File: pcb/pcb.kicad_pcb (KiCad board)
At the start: 2 copper layers, 99.7 x 99.7 mm, 47 parts, among them IC1 TPS63802DLAT, IC2 TUSB320LIRWBR, J1 USB_C_Receptacle_PowerOnly_6P, J2 Soil_Sensor, J3 Pump, J4 Conn_01x03, Q1 2N7002, Q2 AO3401A, Q3 AO3400A, U1 BQ24075RGTR, U2 ESP-32S_USB-C_CH340_DevBoard

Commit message: Testing some KiCAD preview (PCB, Schematic) and checks (ERC, DRC) automation
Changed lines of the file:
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@@
 		(tags "resistor handsolder")
 		(property "Reference" "R14"
-			(at -4.318 0 0)
+			(at 0 2.032 0)
 			(layer "F.SilkS")
 			(effects

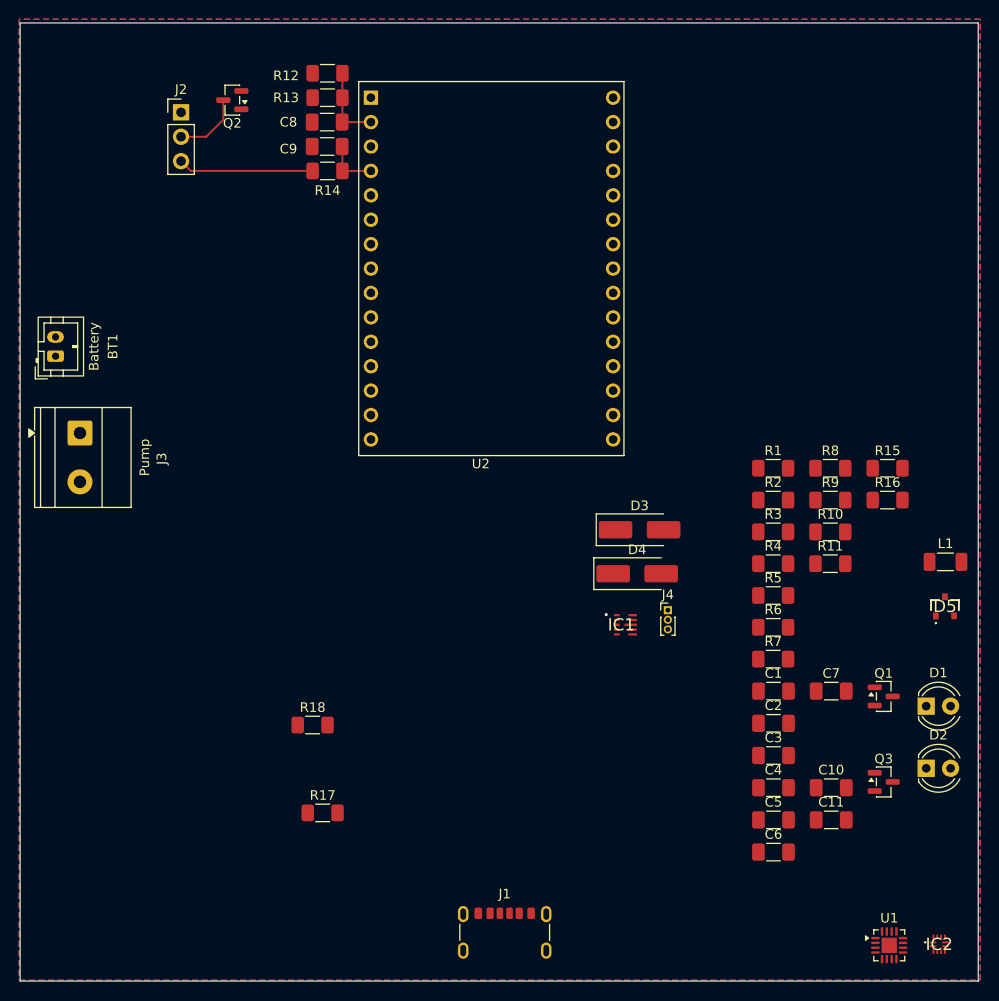
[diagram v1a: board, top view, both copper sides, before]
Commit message: Added a new water level sensor
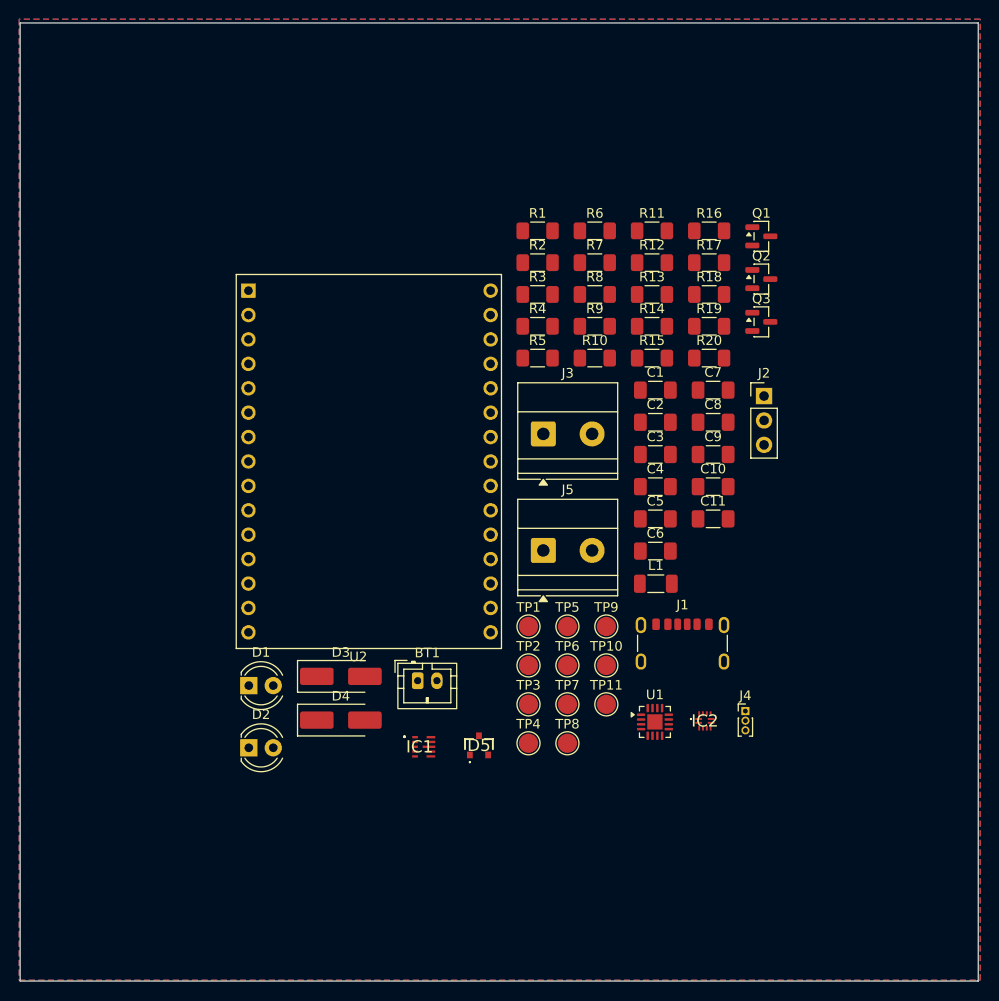
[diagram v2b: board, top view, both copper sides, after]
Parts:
- added J5: Water_Sensor, TerminalBlock_Phoenix:TerminalBlock_Phoenix_MKDS-1,5-2-5.08_1x02_P5.08mm_Horizontal, F.Cu at (154.8, 108.1)
- added R19: 100k, Resistor_SMD:R_1206_3216Metric_Pad1.30x1.75mm_HandSolder, F.Cu at (172.0, 84.7)
- added R20: 1K, Resistor_SMD:R_1206_3216Metric_Pad1.30x1.75mm_HandSolder, F.Cu at (172.0, 88.1)
- added TP1: VBUS, TestPoint:TestPoint_Pad_D2.0mm, F.Cu at (153.2, 116.0)
- added TP10: PUMP_DRAIN, TestPoint:TestPoint_Pad_D2.0mm, F.Cu at (161.3, 120.0)
- added TP11: WATER_OUT, TestPoint:TestPoint_Pad_D2.0mm, F.Cu at (161.3, 124.1)
- added TP2: VIMM, TestPoint:TestPoint_Pad_D2.0mm, F.Cu at (153.2, 120.0)
- added TP3: BAT, TestPoint:TestPoint_Pad_D2.0mm, F.Cu at (153.2, 124.1)
- added TP4: 3.3V, TestPoint:TestPoint_Pad_D2.0mm, F.Cu at (153.2, 128.1)
- added TP5: BAT_SENSE, TestPoint:TestPoint_Pad_D2.0mm, F.Cu at (157.3, 116.0)
- added TP6: SOIL_OUT, TestPoint:TestPoint_Pad_D2.0mm, F.Cu at (157.3, 120.0)
- added TP7: ~{SOIL_ON}, TestPoint:TestPoint_Pad_D2.0mm, F.Cu at (157.3, 124.1)
- added TP8: PUMP_ON, TestPoint:TestPoint_Pad_D2.0mm, F.Cu at (157.3, 128.1)
- added TP9: SOIL_DRAIN, TestPoint:TestPoint_Pad_D2.0mm, F.Cu at (161.3, 116.0)
- BT1: value Battery -> Battery_Cell
- J1: value USB_C_Receptacle_PowerOnly_6P -> USB_C_PowerOnly
- U2: value ESP-32S_USB-C_CH340_DevBoard -> ESP-32S DevBoard
- moved D1 70.5 mm to (124.1, 122.1)
- moved D2 70.5 mm to (124.1, 128.6)
- moved R17 70.0 mm to (172.0, 78.1)
- moved J2 67.5 mm to (177.8, 92.0)
- moved R18 60.9 mm to (172.0, 81.4)
- moved Q2 58.1 mm to (177.5, 79.8), turned to 0 degrees
- moved C9 51.4 mm to (172.5, 98.1), turned to 0 degrees
- moved C8 50.9 mm to (172.5, 94.7), turned to 0 degrees
- moved D5 50.6 mm to (148.1, 128.3)
- moved BT1 50.6 mm to (141.7, 121.6), turned to 0 degrees
- moved Q1 49.5 mm to (177.5, 75.4)
- moved Q3 49.5 mm to (177.5, 84.3)
- moved J3 48.2 mm to (154.8, 95.9), turned to 0 degrees
- moved R6 45.2 mm to (160.1, 74.8)
- moved R7 45.2 mm to (160.1, 78.1)
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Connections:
- U2 pad 20: unconnected-(U2-D21-Pad20) -> WATER_OUT
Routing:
- net Net-(J2-Pin_3): track 14.1 -> 0.00 mm
- net BAT_SENSE: track 8.08 -> 0.00 mm
- net Net-(J2-Pin_2): track 7.16 -> 0.00 mm
- net SOIL_OUT: track 5.52 -> 0.00 mm

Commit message: Refactoring of the library location and startingt o use JLCPCB libraries for components
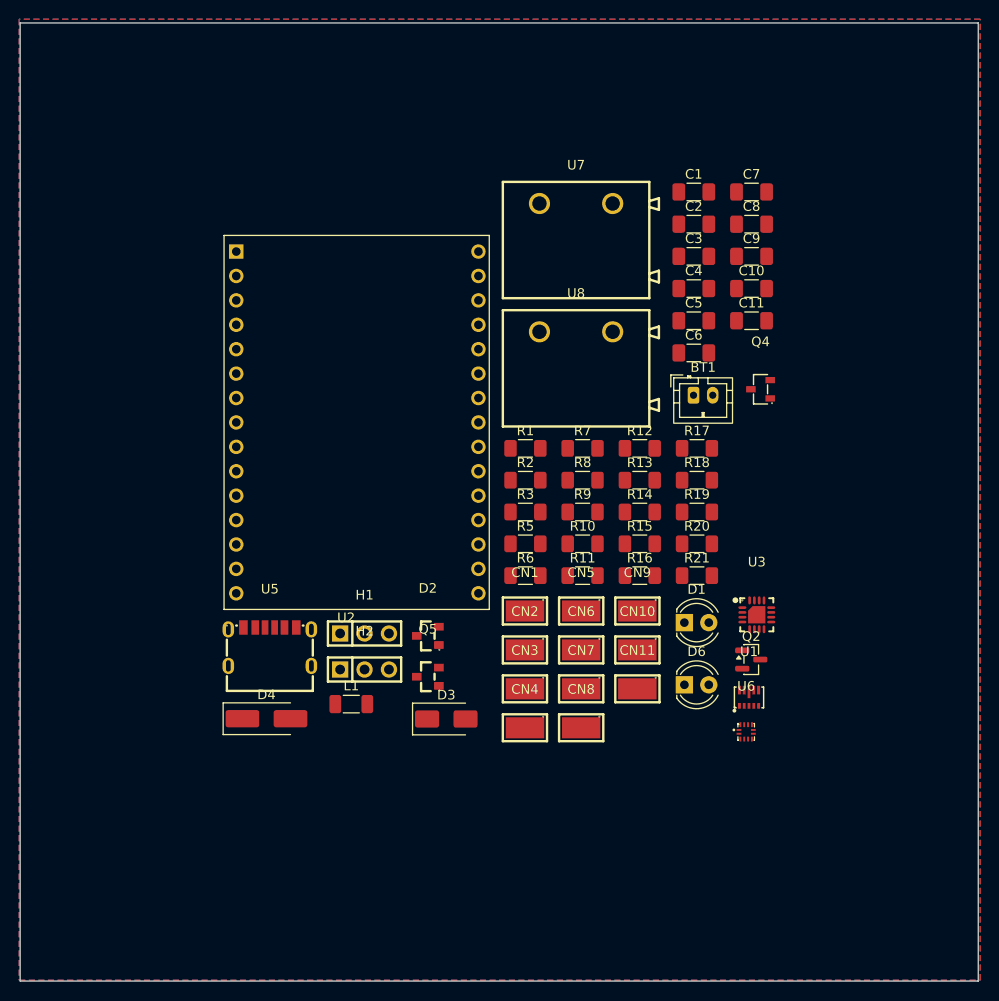
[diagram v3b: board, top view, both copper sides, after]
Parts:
- removed D5: PESD5V0S2BT-QR, SamacSys:PESD5V0S2BTQR
- removed IC1: TPS63802DLAT, SamacSys:TPS63802DLAT
- removed IC2: TUSB320LIRWBR, SamacSys:TUSB320LIRWBR
- removed J1: USB_C_PowerOnly, Connector_USB:USB_C_Receptacle_GCT_USB4125-xx-x-0190_6P_TopMnt_Horizontal
- removed J2: Soil_Sensor, Connector_PinHeader_2.54mm:PinHeader_1x03_P2.54mm_Vertical
- removed J3: Pump, TerminalBlock_Phoenix:TerminalBlock_Phoenix_MKDS-1,5-2-5.08_1x02_P5.08mm_Horizontal
- removed J4: Conn_01x03, Connector_PinHeader_1.00mm:PinHeader_1x03_P1.00mm_Vertical
- removed J5: Water_Sensor, TerminalBlock_Phoenix:TerminalBlock_Phoenix_MKDS-1,5-2-5.08_1x02_P5.08mm_Horizontal
- removed Q1: 2N7002, Package_TO_SOT_SMD:SOT-23
- removed Q3: AO3400A, Package_TO_SOT_SMD:SOT-23
- removed R4: 1.5k, Resistor_SMD:R_1206_3216Metric_Pad1.30x1.75mm_HandSolder
- removed TP1: VBUS, TestPoint:TestPoint_Pad_D2.0mm
- removed TP10: PUMP_DRAIN, TestPoint:TestPoint_Pad_D2.0mm
- removed TP11: WATER_OUT, TestPoint:TestPoint_Pad_D2.0mm
- removed TP2: VIMM, TestPoint:TestPoint_Pad_D2.0mm
- removed TP3: BAT, TestPoint:TestPoint_Pad_D2.0mm
- removed TP4: 3.3V, TestPoint:TestPoint_Pad_D2.0mm
- removed TP5: BAT_SENSE, TestPoint:TestPoint_Pad_D2.0mm
- removed TP6: SOIL_OUT, TestPoint:TestPoint_Pad_D2.0mm
- removed TP7: ~{SOIL_ON}, TestPoint:TestPoint_Pad_D2.0mm
- removed TP8: PUMP_ON, TestPoint:TestPoint_Pad_D2.0mm
- removed TP9: SOIL_DRAIN, TestPoint:TestPoint_Pad_D2.0mm
- added CN1: Pump_Drain, EasyEDA:TESTPOINT-SMD_L3.8-W2.0_RH-5019, F.Cu at (152.9, 114.4)
- added CN10: VIMM, EasyEDA:TESTPOINT-SMD_L3.8-W2.0_RH-5019, F.Cu at (164.6, 118.4)
- added CN11: VBUS, EasyEDA:TESTPOINT-SMD_L3.8-W2.0_RH-5019, F.Cu at (164.6, 122.5)
- added CN2: Soil_Drain, EasyEDA:TESTPOINT-SMD_L3.8-W2.0_RH-5019, F.Cu at (152.9, 118.4)
- added CN3: ~{Soil_On}, EasyEDA:TESTPOINT-SMD_L3.8-W2.0_RH-5019, F.Cu at (152.9, 122.5)
- added CN4: Soil_Out, EasyEDA:TESTPOINT-SMD_L3.8-W2.0_RH-5019, F.Cu at (152.9, 126.5)
- added CN5: Pump_On, EasyEDA:TESTPOINT-SMD_L3.8-W2.0_RH-5019, F.Cu at (158.7, 114.4)
- added CN6: Water_Out, EasyEDA:TESTPOINT-SMD_L3.8-W2.0_RH-5019, F.Cu at (158.7, 118.4)
- added CN7: 3.3V, EasyEDA:TESTPOINT-SMD_L3.8-W2.0_RH-5019, F.Cu at (158.7, 122.5)
- added CN8: Bat_Sense, EasyEDA:TESTPOINT-SMD_L3.8-W2.0_RH-5019, F.Cu at (158.7, 126.5)
- added CN9: Battery, EasyEDA:TESTPOINT-SMD_L3.8-W2.0_RH-5019, F.Cu at (164.6, 114.4)
- added D6: LED, LED_THT:LED_D4.0mm, F.Cu at (169.5, 122.1)
- added H1: Soil_Sensor, EasyEDA:HDR-TH_3P-P2.54-V-M_PZ254V-11-03P, F.Cu at (136.2, 116.7)
- added H2: Power_Select, EasyEDA:HDR-TH_3P-P2.54-V-M_PZ254V-11-03P, F.Cu at (136.2, 120.5)
- added Q4: AO3400A, EasyEDA:SOT-23-3_L2.9-W1.3-P1.90-LS2.4-BR, F.Cu at (177.4, 91.3)
- added Q5: AO3401A, EasyEDA:SOT-23_L2.9-W1.3-P1.90-LS2.4-BR, F.Cu at (142.8, 121.2)
- added R21: 1.5k, Resistor_SMD:R_1206_3216Metric_Pad1.30x1.75mm_HandSolder, F.Cu at (170.8, 110.7)
- added U3: BQ24075RGTR, EasyEDA:QFN-16_L3.0-W3.0-P0.50-TL-EP1.7, F.Cu at (177.0, 114.8)
- added U5: HX TYPE-C 6PIN, EasyEDA:USB-C-SMD_HX-TYPE-C-6PIN, F.Cu at (126.3, 118.1)
- added U6: TUSB320LIRWBR, EasyEDA:X2QFN-12_L1.6-W1.6-P0.40-TL, F.Cu at (175.9, 126.9)
- added U7: Pump, EasyEDA:CONN-TH_MX7620-7.62-02P-GN01-CU-S-A, F.Cu at (158.2, 72.0)
- added U8: Water_Sensor, EasyEDA:CONN-TH_MX7620-7.62-02P-GN01-CU-S-A, F.Cu at (158.2, 85.3)
- D2: value LED -> PESD5V0S2BT,215; footprint LED_THT:LED_D4.0mm -> EasyEDA:SOT-23_L2.9-W1.3-P1.90-LS2.4-BR
- D3: footprint Diode_SMD:D_SMA_Handsoldering -> Diode_SMD:D_SMA
- Q2: value AO3401A -> 2N7002
- U1: value BQ24075RGTR -> TPS63802DLAT; footprint Package_DFN_QFN:VQFN-16-1EP_3x3mm_P0.5mm_EP1.6x1.6mm -> EasyEDA:VSON-10-HR_L3.0-W2.0-P0.50-BL_TI_DLA
- moved D1 45.8 mm to (169.5, 115.6)
- moved BT1 41.3 mm to (170.4, 91.9)
- moved Q2 39.6 mm to (176.4, 119.4)
- moved R11 36.6 mm to (158.9, 110.7)
- moved R16 36.6 mm to (164.8, 110.7)
- moved R6 36.6 mm to (152.9, 110.7)
- moved L1 34.1 mm to (134.8, 124.1)
- moved R1 22.7 mm to (152.9, 97.5)
- moved R2 22.7 mm to (152.9, 100.8)
- moved R3 22.7 mm to (152.9, 104.1)
- moved D2 22.0 mm to (142.8, 117.0)
- moved C1 21.0 mm to (170.4, 70.8)
- moved C10 21.0 mm to (176.5, 80.8)
- moved C2 21.0 mm to (170.4, 74.1)
- moved C4 21.0 mm to (170.4, 80.8)
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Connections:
- D2 pad 1: Net-(D2-K) -> CC1
- D2 pad 2: Net-(D2-A) -> CC2
- L1 pad 1: Net-(IC1-L2) -> Net-(U1-L1)
- L1 pad 2: Net-(IC1-L1) -> Net-(U1-L2)
- Q2 pad 1: Net-(Q2-G) -> EN1
- Q2 pad 2: +3.3V -> GND
- Q2 pad 3: Net-(J2-Pin_2) -> EN2
- R10 pad 1: Net-(IC1-FB) -> Net-(U1-FB)
- R11 pad 2: Net-(IC1-FB) -> Net-(U1-FB)
- R17 pad 2: Net-(Q2-G) -> Net-(Q5-G)
- R18 pad 1: Net-(Q2-G) -> Net-(Q5-G)
- R5 pad 2: Net-(U1-TS) -> Net-(U3-TS)
- R6 pad 1: Net-(U1-ISET) -> Net-(U3-ISET)
- R7 pad 2: Net-(U1-ILIM) -> Net-(U3-ILIM)
- R8 pad 2: Net-(U1-TMR) -> Net-(U3-TMR)
- U1 pad 1: Net-(U1-TS) -> VIMM
- U1 pad 2: Net-(BT1-+) -> GND
- U1 pad 3: Net-(BT1-+) -> GND
- U1 pad 4: GND -> Net-(U1-FB)
- U1 pad 5: EN2 -> unconnected-(U1-PG-Pad5)
- U1 pad 6: EN1 -> +3.3V
- U1 pad 7: Net-(D1-K) -> Net-(U1-L2)
- U1 pad 9: Net-(D2-K) -> Net-(U1-L1)

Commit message: Replaced all the resistors with 0805 LCSC components
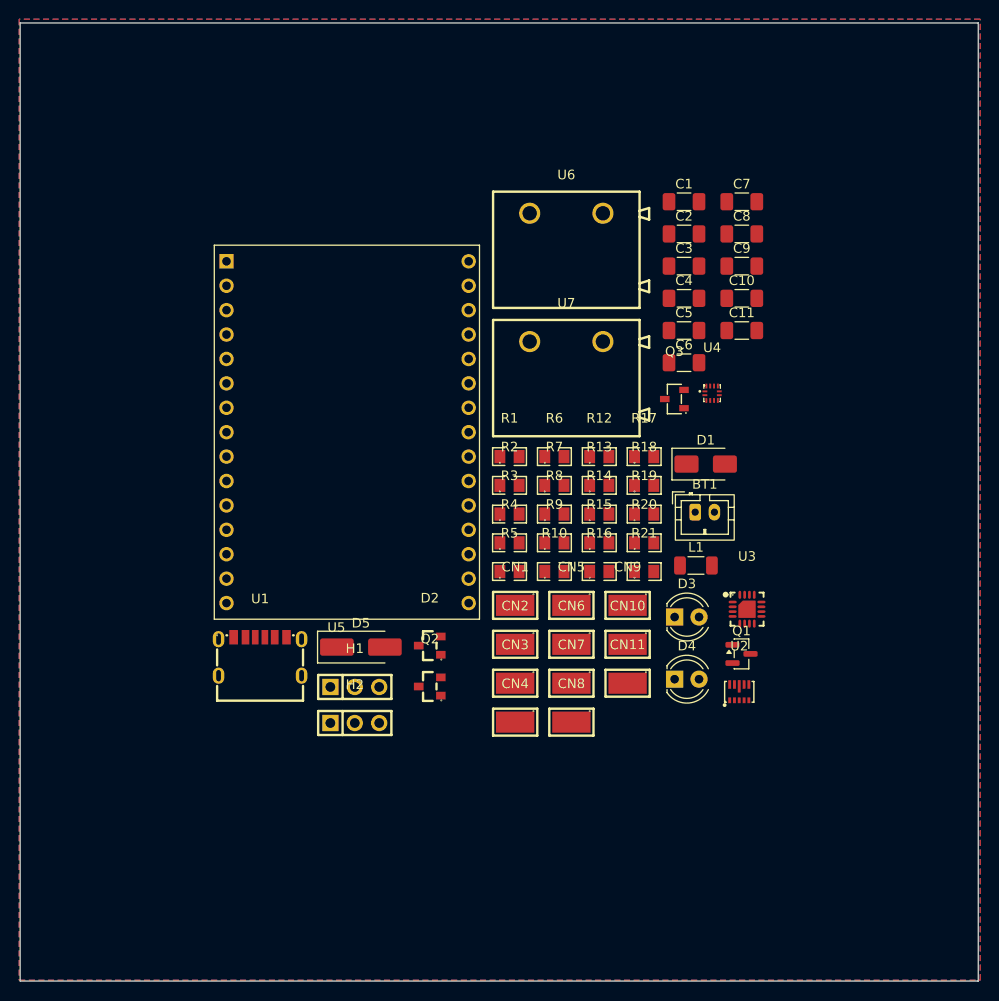
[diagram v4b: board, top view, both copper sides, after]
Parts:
- removed D6: LED, LED_THT:LED_D4.0mm
- removed Q4: AO3400A, EasyEDA:SOT-23-3_L2.9-W1.3-P1.90-LS2.4-BR
- removed Q5: AO3401A, EasyEDA:SOT-23_L2.9-W1.3-P1.90-LS2.4-BR
- removed R11: 91k, Resistor_SMD:R_1206_3216Metric_Pad1.30x1.75mm_HandSolder
- removed U8: Water_Sensor, EasyEDA:CONN-TH_MX7620-7.62-02P-GN01-CU-S-A
- added D5: D_Schottky, Diode_SMD:D_SMA_Handsoldering, F.Cu at (135.8, 118.1)
- added Q1: 2N7002, Package_TO_SOT_SMD:SOT-23, F.Cu at (175.4, 118.8)
- added Q3: AO3400A, EasyEDA:SOT-23-3_L2.9-W1.3-P1.90-LS2.4-BR, F.Cu at (168.4, 92.3)
- added R4: 100k, EasyEDA:R0805, F.Cu at (151.3, 107.3)
- added U4: TUSB320LIRWBR, EasyEDA:X2QFN-12_L1.6-W1.6-P0.40-TL, F.Cu at (172.4, 91.7)
- C1, C4: value 4.7uF -> 100nF
- C2, C7: value 100nF -> 4.7uF
- C3: value 10uF -> 4.7uF
- C5: value 4.7uF -> 10uF
- CN1: value Pump_Drain -> Battery
- CN10: value VIMM -> Pump_On
- CN11: value VBUS -> Pump_Drain
- CN2: value Soil_Drain -> Bat_Sense
- CN3: value ~{Soil_On} -> VBUS
- CN4: value Soil_Out -> 3.3V
- CN5: value Pump_On -> VIMM
- CN6: value Water_Out -> ~{Soil_On}
- CN7: value 3.3V -> Soil_Drain
- CN8: value Bat_Sense -> Soil_Out
- CN9: value Battery -> Water_Out
- D1: value LED -> SMAJ6.0A; footprint LED_THT:LED_D4.0mm -> Diode_SMD:D_SMA
- D3: value SMAJ6.0A -> LED; footprint Diode_SMD:D_SMA -> LED_THT:LED_D4.0mm
- D4: value D_Schottky -> LED; footprint Diode_SMD:D_SMA_Handsoldering -> LED_THT:LED_D4.0mm
- H1: value Soil_Sensor -> Power_Select
- H2: value Power_Select -> Soil_Sensor
- Q2: value 2N7002 -> AO3401A; footprint Package_TO_SOT_SMD:SOT-23 -> EasyEDA:SOT-23_L2.9-W1.3-P1.90-LS2.4-BR
- R1: value 900k -> 511k; footprint Resistor_SMD:R_1206_3216Metric_Pad1.30x1.75mm_HandSolder -> EasyEDA:R0805
- R10: value 511k -> 47k; footprint Resistor_SMD:R_1206_3216Metric_Pad1.30x1.75mm_HandSolder -> EasyEDA:R0805
- R12, R13: value 100k -> 1.5k; footprint Resistor_SMD:R_1206_3216Metric_Pad1.30x1.75mm_HandSolder -> EasyEDA:R0805
- R14, R5, R7, R9: footprint Resistor_SMD:R_1206_3216Metric_Pad1.30x1.75mm_HandSolder -> EasyEDA:R0805
- R15: value 100 -> 100k; footprint Resistor_SMD:R_1206_3216Metric_Pad1.30x1.75mm_HandSolder -> EasyEDA:R0805
- R16: value 10k -> 1k; footprint Resistor_SMD:R_1206_3216Metric_Pad1.30x1.75mm_HandSolder -> EasyEDA:R0805
- R17: value 1k -> 100k; footprint Resistor_SMD:R_1206_3216Metric_Pad1.30x1.75mm_HandSolder -> EasyEDA:R0805
- R18: value 100k -> 1k; footprint Resistor_SMD:R_1206_3216Metric_Pad1.30x1.75mm_HandSolder -> EasyEDA:R0805
- R19: value 100k -> 100; footprint Resistor_SMD:R_1206_3216Metric_Pad1.30x1.75mm_HandSolder -> EasyEDA:R0805
- R2: value 47k -> 91k; footprint Resistor_SMD:R_1206_3216Metric_Pad1.30x1.75mm_HandSolder -> EasyEDA:R0805
- R20: value 1K -> 10k; footprint Resistor_SMD:R_1206_3216Metric_Pad1.30x1.75mm_HandSolder -> EasyEDA:R0805
- R21: value 1.5k -> 900k; footprint Resistor_SMD:R_1206_3216Metric_Pad1.30x1.75mm_HandSolder -> EasyEDA:R0805
- R3: value 1.5k -> 100k; footprint Resistor_SMD:R_1206_3216Metric_Pad1.30x1.75mm_HandSolder -> EasyEDA:R0805
- R6: value 2.2k -> 56.2k; footprint Resistor_SMD:R_1206_3216Metric_Pad1.30x1.75mm_HandSolder -> EasyEDA:R0805
- R8: value 56.2k -> 2.2k; footprint Resistor_SMD:R_1206_3216Metric_Pad1.30x1.75mm_HandSolder -> EasyEDA:R0805
- U1: value TPS63802DLAT -> USB-C 6PIN; footprint EasyEDA:VSON-10-HR_L3.0-W2.0-P0.50-BL_TI_DLA -> EasyEDA:USB-C-SMD_HX-TYPE-C-6PIN
- U2: value ESP-32S DevBoard -> TPS63802DLAT; footprint pcb:ESP-32S_USB-C_CH340_DevBoard -> EasyEDA:VSON-10-HR_L3.0-W2.0-P0.50-BL_TI_DLA
- U5: value HX TYPE-C 6PIN -> ESP-32S DevBoard; footprint EasyEDA:USB-C-SMD_HX-TYPE-C-6PIN -> pcb:ESP-32S_USB-C_CH340_DevBoard
- U6: value TUSB320LIRWBR -> Water_Sensor; footprint EasyEDA:X2QFN-12_L1.6-W1.6-P0.40-TL -> EasyEDA:CONN-TH_MX7620-7.62-02P-GN01-CU-S-A
- moved U2 69.6 mm to (175.2, 122.8)
- moved U6 57.1 mm to (157.2, 73.0)
- moved U1 51.1 mm to (125.3, 119.1)
- moved D4 42.7 mm to (168.5, 121.5)
- moved U5 40.4 mm to (121.8, 78.0)
- moved L1 38.7 mm to (170.7, 109.6)
- moved Q2 33.6 mm to (143.0, 122.2)
- moved D3 26.0 mm to (168.5, 115.0)
- moved D1 16.6 mm to (171.7, 99.1)
- moved U7 14.4 mm to (157.2, 86.3)
- moved R6 12.7 mm to (155.9, 98.3)
- moved BT1 12.2 mm to (170.6, 104.1)
- moved H1 5.66 mm to (135.2, 122.3)
- moved H2 5.66 mm to (135.2, 126.0)
- moved R17 5.56 mm to (165.3, 98.3)
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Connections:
- C1 pad 1: GND -> BAT_SENSE
- C1 pad 2: VBUS -> GND
- C3 pad 1: GND -> Net-(BT1-+)
- C3 pad 2: VIMM -> GND
- C4 pad 1: VIMM -> GND
- C4 pad 2: GND -> VBUS
- C5 pad 1: Net-(BT1-+) -> GND
- C5 pad 2: GND -> VIMM
- C7 pad 1: GND -> VIMM
- C7 pad 2: +3.3V -> GND
- C8 pad 1: BAT_SENSE -> GND
- C8 pad 2: GND -> +3.3V
- CN1 pad 1: Net-(D4-A) -> Net-(BT1-+)
- CN10 pad 1: VIMM -> PUMP_ON
- CN11 pad 1: VBUS -> Net-(D5-A)
- CN2 pad 1: Net-(Q5-D) -> BAT_SENSE
- CN3 pad 1: ~{SOIL_ON} -> VBUS
- CN4 pad 1: SOIL_OUT -> +3.3V
- CN5 pad 1: PUMP_ON -> VIMM
- CN6 pad 1: WATER_OUT -> ~{SOIL_ON}
- CN7 pad 1: +3.3V -> Net-(Q2-D)
- CN8 pad 1: BAT_SENSE -> SOIL_OUT
- CN9 pad 1: Net-(BT1-+) -> WATER_OUT
- D1 pad 1: Net-(D1-K) -> VBUS
- D1 pad 2: Net-(D1-A) -> GND
- D3 pad 1: VBUS -> Net-(D3-K)
- D3 pad 2: GND -> Net-(D3-A)
- D4 pad 1: +3.3V -> Net-(D4-K)
- H1 pad 1: GND -> +3.3V
- H1 pad 2: Net-(Q5-D) -> Net-(U5-3V3)
- H1 pad 3: Net-(H1-Pad3) -> unconnected-(H1-Pad3)
- H2 pad 1: +3.3V -> GND
- H2 pad 2: Net-(U2-3V3) -> Net-(Q2-D)
- H2 pad 3: unconnected-(H2-Pad3) -> Net-(H2-Pad3)
- L1 pad 1: Net-(U1-L1) -> Net-(U2-L1)
- L1 pad 2: Net-(U1-L2) -> Net-(U2-L2)
- Q2 pad 1: EN1 -> Net-(Q2-G)
- Q2 pad 2: GND -> +3.3V
- Q2 pad 3: EN2 -> Net-(Q2-D)
- R1 pad 1: VBUS -> Net-(U2-FB)
- R1 pad 2: Net-(U6-VBUS_DET) -> +3.3V
- R10 pad 1: Net-(U1-FB) -> +3.3V
- R10 pad 2: +3.3V -> EN1
- R12 pad 1: Net-(BT1-+) -> Net-(D3-A)
- R12 pad 2: BAT_SENSE -> VIMM
- R13 pad 1: BAT_SENSE -> Net-(D4-A)
- R13 pad 2: GND -> VIMM
- R14 pad 1: Net-(H1-Pad3) -> ~{SOIL_ON}
- R14 pad 2: SOIL_OUT -> Net-(Q2-G)
- R15 pad 1: PUMP_ON -> +3.3V
- R15 pad 2: Net-(Q4-G) -> Net-(Q2-G)
- R16 pad 1: Net-(Q4-G) -> Net-(H2-Pad3)
- R16 pad 2: GND -> SOIL_OUT
- R17 pad 1: ~{SOIL_ON} -> WATER_OUT
- R17 pad 2: Net-(Q5-G) -> +3.3V
- R18 pad 1: Net-(Q5-G) -> Net-(R18-Pad1)
- R18 pad 2: +3.3V -> WATER_OUT
- R19 pad 1: +3.3V -> PUMP_ON
- R19 pad 2: WATER_OUT -> Net-(Q3-G)
- R2 pad 1: EN2 -> GND
- R2 pad 2: +3.3V -> Net-(U2-FB)
- R20 pad 1: WATER_OUT -> GND
- R20 pad 2: Net-(R20-Pad2) -> Net-(Q3-G)
- R21 pad 1: VIMM -> VBUS
- R3 pad 1: VIMM -> BAT_SENSE
- R3 pad 2: Net-(D1-A) -> Net-(BT1-+)
- R6 pad 1: Net-(U3-ISET) -> GND
- R6 pad 2: GND -> Net-(U3-TMR)
- R8 pad 2: Net-(U3-TMR) -> Net-(U3-ISET)
- R9 pad 1: EN1 -> +3.3V
- R9 pad 2: +3.3V -> EN2
- U2 pad 1: unconnected-(U2-EN-Pad1) -> VIMM
- U2 pad 10: unconnected-(U2-D27-Pad10) -> VIMM
- U2 pad 2: BAT_SENSE -> GND
- U2 pad 3: unconnected-(U2-VN-Pad3) -> GND
- U2 pad 4: SOIL_OUT -> Net-(U2-FB)
- U2 pad 6: ~{SOIL_ON} -> +3.3V
- U2 pad 7: unconnected-(U2-D33-Pad7) -> Net-(U2-L2)
- U2 pad 8: unconnected-(U2-D25-Pad8) -> GND
- U2 pad 9: unconnected-(U2-D26-Pad9) -> Net-(U2-L1)
- U3 pad 7: Net-(D1-K) -> Net-(D4-K)
- U3 pad 9: Net-(D6-K) -> Net-(D3-K)
- U5 pad 13: GND -> unconnected-(U5-D13-Pad13)
- U5 pad 15: GND -> unconnected-(U5-VIN-Pad15)
- U5 pad 16: GND -> unconnected-(U5-D23-Pad16)
- U6 pad 1: CC1 -> GND
- U6 pad 2: CC2 -> Net-(R18-Pad1)
- U7 pad 1: Net-(D4-A) -> Net-(D5-A)
